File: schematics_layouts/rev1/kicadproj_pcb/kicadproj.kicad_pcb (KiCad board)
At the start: 2 copper layers, 81.3 x 50.8 mm, 16 parts, among them J1 DS3231_board, J2 LM386_board, J3 microSD_board, Q1 Si2323DS_on_TO220, Q2 Si2323DS_on_TO220, SW1 WAKE Switch, SW2 SET 15MIN, U2 ATmega328P-PU

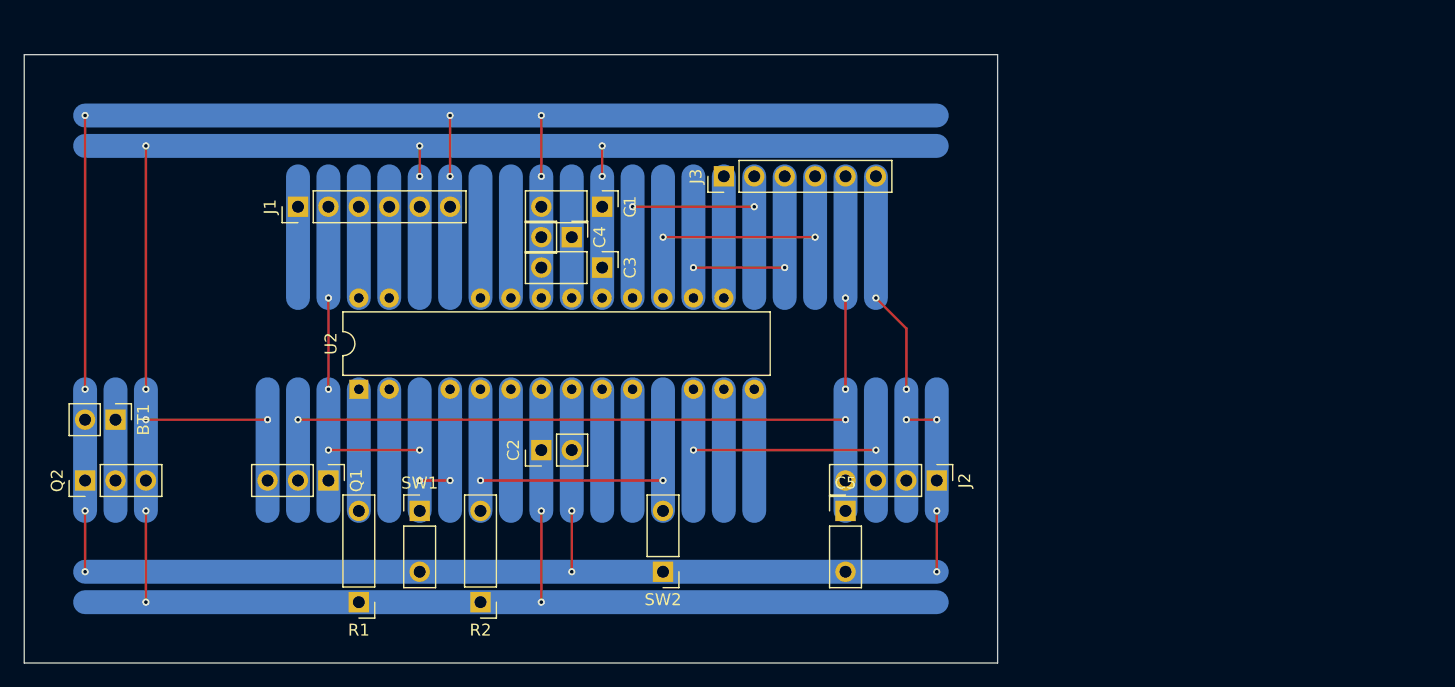
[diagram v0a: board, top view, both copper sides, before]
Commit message: Revised PCB layout; Updated documentation
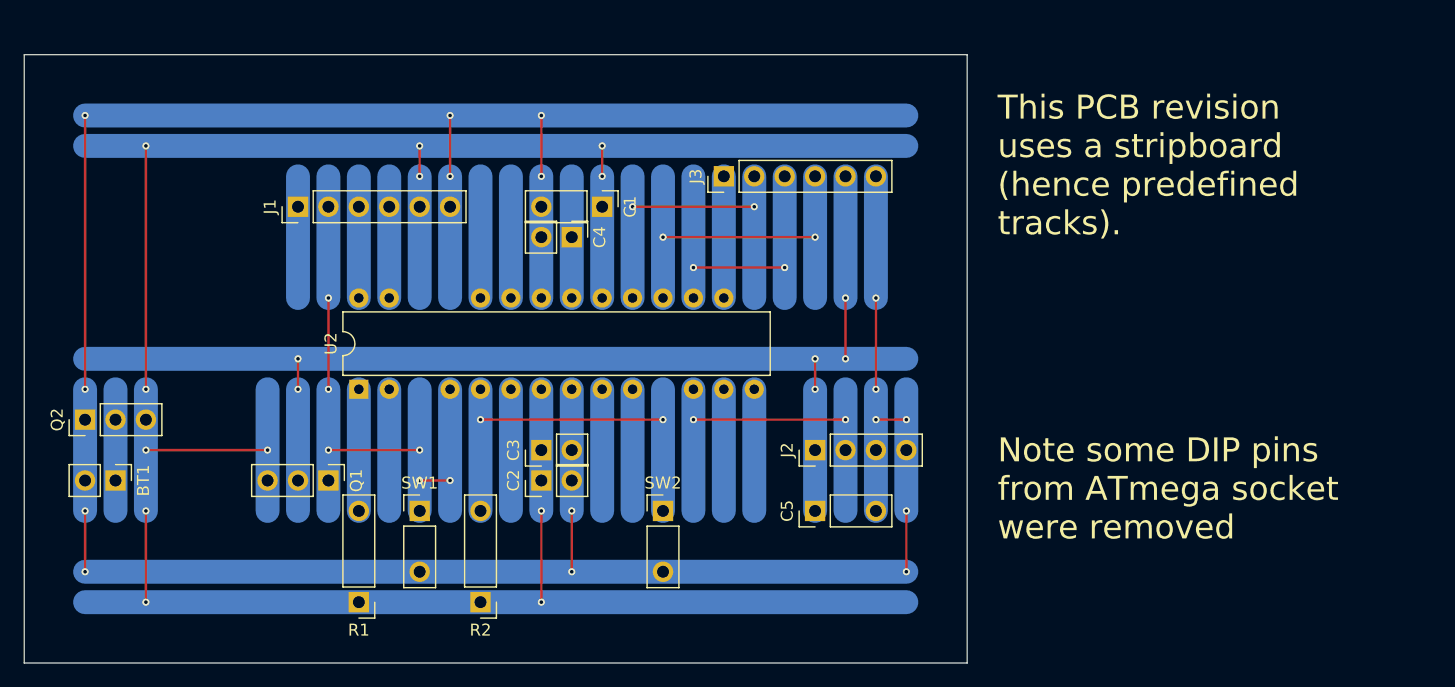
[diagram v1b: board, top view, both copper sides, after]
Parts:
- C3: footprint Connector_PinHeader_2.54mm:PinHeader_1x03_P2.54mm_Vertical -> Connector_PinHeader_2.54mm:PinHeader_1x02_P2.54mm_Vertical
- moved C3 16.1 mm to (142.2, 111.8), turned to 90 degrees
- moved J2 10.5 mm to (165.1, 111.8), turned to 90 degrees
- moved BT1 5.08 mm to (106.7, 114.3)
- moved Q2 5.08 mm to (104.1, 109.2)
- moved SW2 5.08 mm to (152.4, 116.8), turned to 0 degrees
- moved C2 2.54 mm to (142.2, 114.3)
- moved C5 2.54 mm to (165.1, 116.8), turned to 90 degrees
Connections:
- BT1 pad 1: /+BATT0 -> Net-(BT1-Pin_1)
- J2 pad 1: GND -> VCC
- J2 pad 2: GND -> /VIN
- J2 pad 3: /VIN -> GND
- J2 pad 4: VCC -> GND
- Q1 pad 2: VCC -> /+BATT
- Q1 pad 3: /+BATT -> VCC
- Q2 pad 2: /+BATT0 -> /+BATT
- Q2 pad 3: /+BATT -> Net-(BT1-Pin_1)
- R2 pad 4: Net-(SW2-2) -> Net-(U2-Pin_5)
- SW2 pad 1: GND -> Net-(U2-Pin_5)
- SW2 pad 3: Net-(SW2-2) -> GND
- U2 pad 5: Net-(SW2-2) -> Net-(U2-Pin_5)
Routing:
- net Net-(SW2-2): track 35.6 -> 0.00 mm, vias 2 -> 0
- net GND: track 272.8 -> 251.5 mm
- net Net-(U2-Pin_5): track 0.00 -> 20.3 mm, vias 0 -> 2
- net VCC: track 83.8 -> 101.6 mm, vias 4 -> 6
- net /VIN: track 35.6 -> 20.3 mm
- net Net-(BT1-Pin_1): track 0.00 -> 10.2 mm
- net /+BATT0: track 10.2 -> 0.00 mm
- net /+BATT: track 243.8 -> 238.8 mm
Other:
- board size 81.3 x 50.8 mm -> 78.7 x 50.8 mm
- board text added: "Note some DIP pins from ATmega socket were removed"
- board text added: "This PCB revision uses a stripboard (hence predefined tracks)."

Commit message: Revised PCB layout; Created PCB layout revision 1b
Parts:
- moved Q2 7.62 mm to (111.8, 109.2)
- moved BT1 7.62 mm to (114.3, 114.3)
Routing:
- net /+BATT: track 238.8 -> 215.9 mm
- net GND: track 251.5 -> 236.2 mm
- net VCC: track 101.6 -> 94.0 mm
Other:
- board size 78.7 x 50.8 mm -> 71.1 x 50.8 mm
- board text added: "Rev. 1"

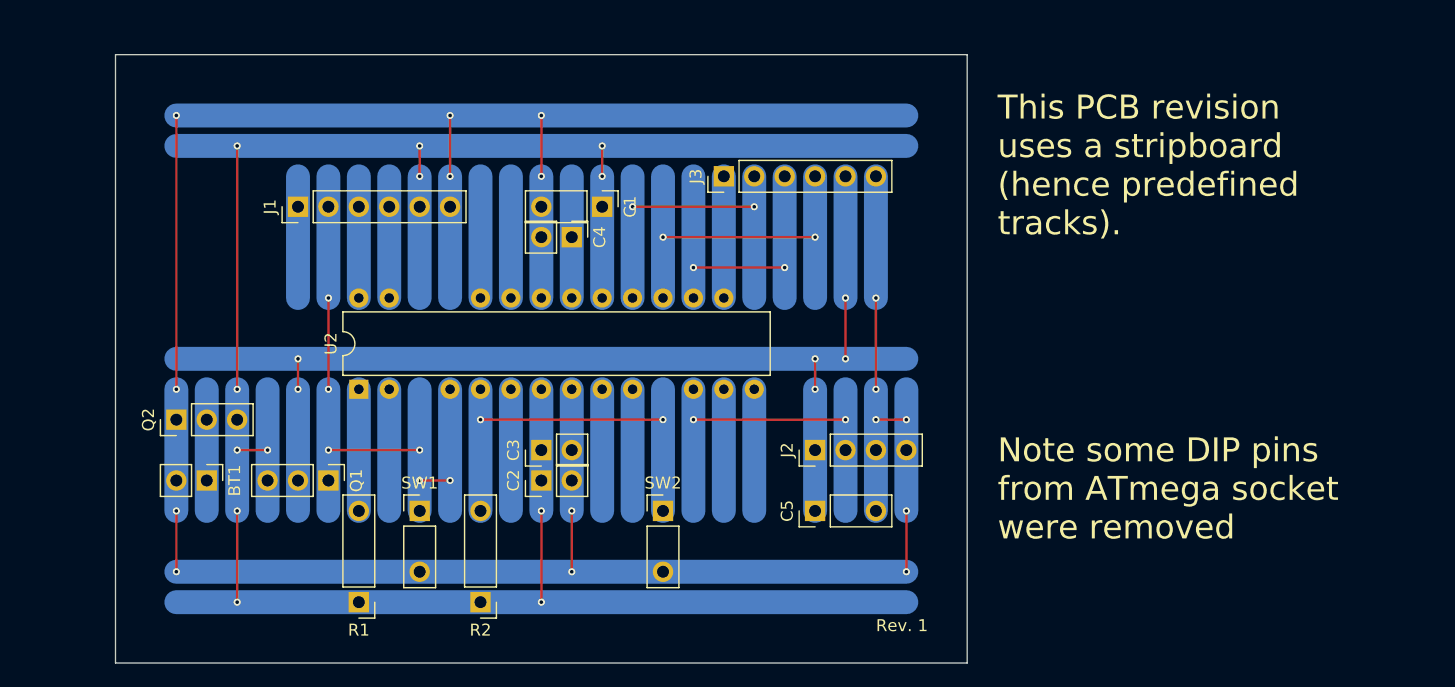
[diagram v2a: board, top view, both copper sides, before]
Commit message: Revised PCB layouts; Created PCB layout revision 1c; Updated docs
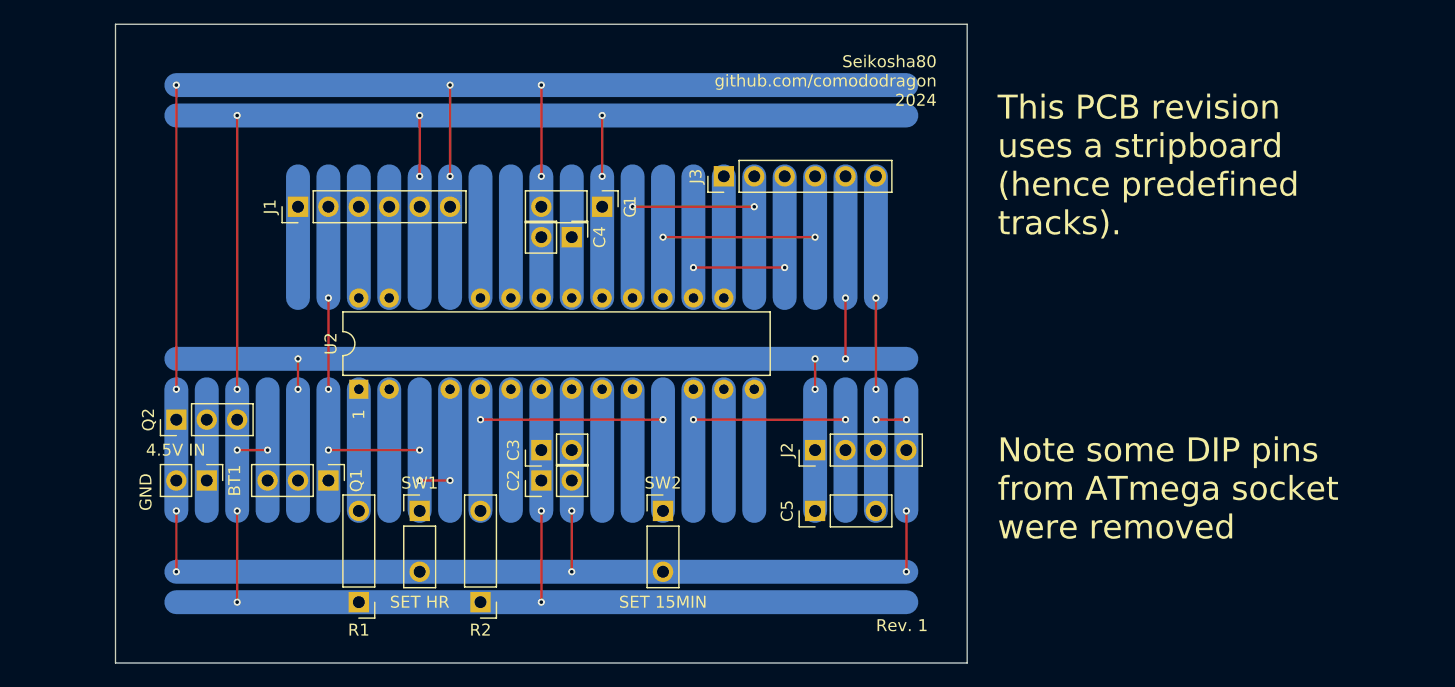
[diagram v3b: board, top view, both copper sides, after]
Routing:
- net /+BATT: track 215.9 -> 223.5 mm
- net GND: track 236.2 -> 243.8 mm
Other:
- board size 71.1 x 50.8 mm -> 71.1 x 53.3 mm
- board text added: "1"
- board text added: "4.5V IN"
- board text added: "GND"
- board text added: "SET 15MIN"
- board text added: "SET HR"
- board text added: "Seikosha80 github.com/comododragon 2024"
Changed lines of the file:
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@@
 	)
 	(gr_rect
-		(start 106.68 78.74)
+		(start 106.68 76.2)
 		(end 177.8 129.54)
 		(stroke
@@
 		(layer "Edge.Cuts")
 	)
+	(gr_text "4.5V IN"
+		(at 109.22 111.76 0)
+		(layer "F.SilkS")
+		(effects
+			(font
+				(size 1 1)
+				(thickness 0.1)
+			)
+			(justify left)
+		)
+	)
 	(gr_text "This PCB revision\nuses a stripboard\n(hence predefined\ntracks)."
 		(at 180.34 93.98 0)
@@
 		)
 	)
+	(gr_text "1"
+		(at 127 109.22 90)
+		(layer "F.SilkS")
+		(effects
+			(font
+				(size 1 1)
+				(thickness 0.1)
+			)
+			(justify left)
+		)
+	)
 	(gr_text "Note some DIP pins\nfrom ATmega socket\nwere removed"
 		(at 180.34 119.38 0)
@@
 		)
 	)
+	(gr_text "GND"
+		(at 109.22 116.84 90)
+		(layer "F.SilkS")
+		(effects
+			(font
+				(size 1 1)
+				(thickness 0.1)
+			)
+			(justify left)
+		)
+	)
+	(gr_text "Seikosha80\ngithub.com/comododragon\n2024"
+		(at 175.26 78.74 0)
+		(layer "F.SilkS")
+		(effects
+			(font
+				(size 1 1)
+				(thickness 0.1)
+			)
+			(justify right top)
+		)
+	)
+	(gr_text "SET HR"
+		(at 132.08 124.46 0)
+		(layer "F.SilkS")
+		(effects
+			(font
+				(size 1 1)
+				(thickness 0.1)
+			)
+		)
+	)
 	(gr_text "Rev. 1"
 		(at 170.18 127 0)
@@
 		)
 	)
-	(segment
-		(start 111.76 83.82)
-		(end 111.76 106.68)
+	(gr_text "SET 15MIN"
+		(at 152.4 124.46 0)
+		(layer "F.SilkS")
+		(effects
+			(font
+				(size 1 1)
+				(thickness 0.1)
+			)
+		)
+	)
+	(gr_text_box "Revision"
+		(start 193.04 124.46)
+		(end 241.3 129.54)
+		(layer "F.Cu")
+		(effects
+			(font
+				(size 1.5 1.5)
+				(thickness 0.3)
+				(bold yes)
+			)
+			(justify left top)
+		)
+		(border yes)
+		(stroke
+			(width 0.2)
+			(type solid)
+		)
+	)
+	(gr_text_box "Rev. 1: Compact PCB\nRev. 1b: Optimised for daughter cards\nRev. 1c: Optimised for buttons placement"
+		(start 193.04 129.54)
+		(end 241.3 144.78)
+		(layer "F.Cu")
+		(effects
+			(font
+				(size 1.5 1.5)
+				(thickness 0.3)
+				(bold yes)
+			)
+			(justify left top)
+		)
+		(border yes)
+		(stroke
+			(width 0.2)
+			(type solid)
+		)
+	)
+	(segment
+		(start 142.24 81.28)
+		(end 142.24 88.9)
 		(width 0.2)
 		(layer "F.Cu")
@@
 	)
 	(segment
+		(start 111.76 81.28)
+		(end 111.76 106.68)
+		(width 0.2)
+		(layer "F.Cu")
+		(net 1)
+	)
+	(segment
 		(start 144.78 116.84)
 		(end 144.78 121.92)
@@
 	)
 	(segment
-		(start 134.62 83.82)
+		(start 134.62 81.28)
 		(end 134.62 88.9)
 		(width 0.2)
@@
 		(net 1)
 	)
-	(segment
-		(start 142.24 83.82)
-		(end 142.24 88.9)
-		(width 0.2)
-		(layer "F.Cu")
-		(net 1)
-	)
-	(via
-		(at 142.24 83.82)
+	(via
+		(at 142.24 81.28)
 		(size 0.6)
 		(drill 0.3)
@@
 	)
 	(via
-		(at 111.76 83.82)
+		(at 111.76 81.28)
 		(size 0.6)
 		(drill 0.3)
@@
 	)
 	(via
-		(at 134.62 83.82)
+		(at 134.62 81.28)
 		(size 0.6)
 		(drill 0.3)
@@
 	)
 	(segment
+		(start 111.76 81.28)
+		(end 172.72 81.28)
+		(width 2)
+		(layer "B.Cu")
+		(net 1)
+	)
+	(segment
 		(start 142.24 99.06)
 		(end 142.24 88.9)
@@
 	)
 	(segment
-		(start 111.76 83.82)
-		(end 172.72 83.82)
-		(width 2)
-		(layer "B.Cu")
-		(net 1)
-	)
-	(segment
 		(start 111.76 106.68)
 		(end 111.76 116.84)
@@
 	)
 	(segment
-		(start 116.84 106.68)
-		(end 116.84 86.36)
-		(width 0.2)
-		(layer "F.Cu")
-		(net 2)
-	)
-	(segment
-		(start 147.32 86.36)
-		(end 147.32 88.9)
-		(width 0.2)
-		(layer "F.Cu")
-		(net 2)
-	)
-	(segment
 		(start 116.84 111.76)
 		(end 119.38 111.76)
@@
 	)
 	(segment
-		(start 132.08 86.36)
+		(start 132.08 83.82)
 		(end 132.08 88.9)
+		(width 0.2)
+		(layer "F.Cu")
+		(net 2)
+	)
+	(segment
+		(start 147.32 83.82)
+		(end 147.32 88.9)
 		(width 0.2)
 		(layer "F.Cu")
@@
 	)
 	(segment
+		(start 116.84 106.68)
+		(end 116.84 83.82)
+		(width 0.2)
+		(layer "F.Cu")
+		(net 2)
+	)
+	(segment
 		(start 142.24 116.84)
 		(end 142.24 124.46)
@@
 	)
 	(via
-		(at 147.32 86.36)
+		(at 147.32 83.82)
 		(size 0.6)
 		(drill 0.3)
@@
 	)
 	(via
-		(at 116.84 86.36)
+		(at 116.84 83.82)
 		(size 0.6)
 		(drill 0.3)
@@
 	)
 	(via
-		(at 132.08 86.36)
+		(at 132.08 83.82)
 		(size 0.6)
 		(drill 0.3)
@@
 	)
 	(segment
-		(start 172.72 86.36)
-		(end 111.76 86.36)
-		(width 2)
-		(layer "B.Cu")
+		(start 172.72 83.82)
+		(end 111.76 83.82)
+		(width 2)
+		(layer "B.Cu")

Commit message: Revised all docs, removed C5 (never heard about it); Updated wiki with some news
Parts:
- removed C5: 100u, Connector_PinHeader_2.54mm:PinHeader_1x03_P2.54mm_Vertical
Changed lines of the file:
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@@
-		)
-	)
-	(footprint "Connector_PinHeader_2.54mm:PinHeader_1x03_P2.54mm_Vertical"
-		(layer "F.Cu")
-		(at 165.1 116.84 90)
-		(descr "Through hole straight pin header, 1x03, 2.54mm pitch, single row")
-		(tags "Through hole pin header THT 1x03 2.54mm single row")
-		(property "Reference" "C5"
-			(at 0 -2.33 -90)
-			(layer "F.SilkS")
-			(effects
-				(font
-					(size 1 1)
-					(thickness 0.15)
-				)
-			)
-		)
-		(property "Value" "100u"
-			(at 0 7.41 -90)
-			(layer "F.Fab")
-			(effects
-				(font
-					(size 1 1)
-					(thickness 0.15)
-				)
-			)
-		)
-		(property "Footprint" "Connector_PinHeader_2.54mm:PinHeader_1x03_P2.54mm_Vertical"
-			(at 0 0 90)
-			(unlocked yes)
-			(layer "F.Fab")
-			(hide yes)
-			(effects
-				(font
-					(size 1.27 1.27)
-				)
-			)
-		)
-		(property "Datasheet" ""
-			(at 0 0 90)
-			(unlocked yes)
-			(layer "F.Fab")
-			(hide yes)
-			(effects
-				(font
-					(size 1.27 1.27)
-				)
-			)
-		)
-		(property "Description" "Polarized capacitor"
-			(at 0 0 90)
-			(unlocked yes)
-			(layer "F.Fab")
-			(hide yes)
-			(effects
-				(font
-					(size 1.27 1.27)
-				)
-			)
-		)
-		(property ki_fp_filters "CP_*")
-		(sheetname "Root")
-		(sheetfile "kicadproj.kicad_sch")
-		(attr through_hole)
-		(fp_line
-			(start -1.33 -1.33)
-			(end 0 -1.33)
-			(stroke
-				(width 0.12)
-				(type solid)
-			)
-			(layer "F.SilkS")
-		)
-		(fp_line
-			(start -1.33 0)
-			(end -1.33 -1.33)
-			(stroke
-				(width 0.12)
-				(type solid)
-			)
-			(layer "F.SilkS")
-		)
-		(fp_line
-			(start 1.33 1.27)
-			(end 1.33 6.41)
-			(stroke
-				(width 0.12)
-				(type solid)
-			)
-			(layer "F.SilkS")
-		)
-		(fp_line
-			(start -1.33 1.27)
-			(end 1.33 1.27)
-			(stroke
-				(width 0.12)
-				(type solid)
-			)
-			(layer "F.SilkS")
-		)
-		(fp_line
-			(start -1.33 1.27)
-			(end -1.33 6.41)
-			(stroke
-				(width 0.12)
-				(type solid)
-			)
-			(layer "F.SilkS")
-		)
-		(fp_line
-			(start -1.33 6.41)
-			(end 1.33 6.41)
-			(stroke
-				(width 0.12)
-				(type solid)
-			)
-			(layer "F.SilkS")
-		)
-		(fp_line
-			(start 1.8 -1.8)
-			(end -1.8 -1.8)
-			(stroke
-				(width 0.05)
-				(type solid)
-			)
-			(layer "F.CrtYd")
-		)
-		(fp_line
-			(start -1.8 -1.8)
-			(end -1.8 6.85)
-			(stroke
-				(width 0.05)
-				(type solid)
-			)
-			(layer "F.CrtYd")
-		)
-		(fp_line
-			(start 1.8 6.85)
-			(end 1.8 -1.8)
-			(stroke
-				(width 0.05)
-				(type solid)
-			)
-			(layer "F.CrtYd")
-		)
-		(fp_line
-			(start -1.8 6.85)
-			(end 1.8 6.85)
-			(stroke
-				(width 0.05)
-				(type solid)
-			)
-			(layer "F.CrtYd")
-		)
-		(fp_line
-			(start 1.27 -1.27)
-			(end 1.27 6.35)
-			(stroke
-				(width 0.1)
-				(type solid)
-			)
-			(layer "F.Fab")
-		)
-		(fp_line
-			(start -0.635 -1.27)
-			(end 1.27 -1.27)
-			(stroke
-				(width 0.1)
-				(type solid)
-			)
-			(layer "F.Fab")
-		)
-		(fp_line
-			(start -1.27 -0.635)
-			(end -0.635 -1.27)
-			(stroke
-				(width 0.1)
-				(type solid)
-			)
-			(layer "F.Fab")
-		)
-		(fp_line
-			(start 1.27 6.35)
-			(end -1.27 6.35)
-			(stroke
-				(width 0.1)
-				(type solid)
-			)
-			(layer "F.Fab")
-		)
-		(fp_line
-			(start -1.27 6.35)
-			(end -1.27 -0.635)
-			(stroke
-				(width 0.1)
-				(type solid)
-			)
-			(layer "F.Fab")
-		)
-		(fp_text user "${REFERENCE}"
-			(at 0 2.54 0)
-			(layer "F.Fab")
-			(effects
-				(font
-					(size 1 1)
-					(thickness 0.15)
-				)
-			)
-		)
-		(pad "1" thru_hole rect
-			(at 0 0 90)
-			(size 1.7 1.7)
-			(drill 1)
-			(layers "*.Cu" "*.Mask")
-			(remove_unused_layers no)
-			(net 4 "VCC")
-			(pintype "passive")
-		)
-		(pad "3" thru_hole oval
-			(at 0 5.08 90)
-			(size 1.7 1.7)
-			(drill 1)
-			(layers "*.Cu" "*.Mask")
-			(remove_unused_layers no)
-			(net 1 "GND")
-			(pintype "passive")
-		)
-		(model "${KISYS3DMOD}/Connector_PinHeader_2.54mm.3dshapes/PinHeader_1x03_P2.54mm_Vertical.wrl"
-			(offset
-				(xyz 0 0 0)
-			)
-			(scale
-				(xyz 1 1 1)
-			)
-			(rotate
-				(xyz 0 0 0)
-			)
 		)
 	)
